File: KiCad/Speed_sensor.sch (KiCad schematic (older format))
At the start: 31 parts

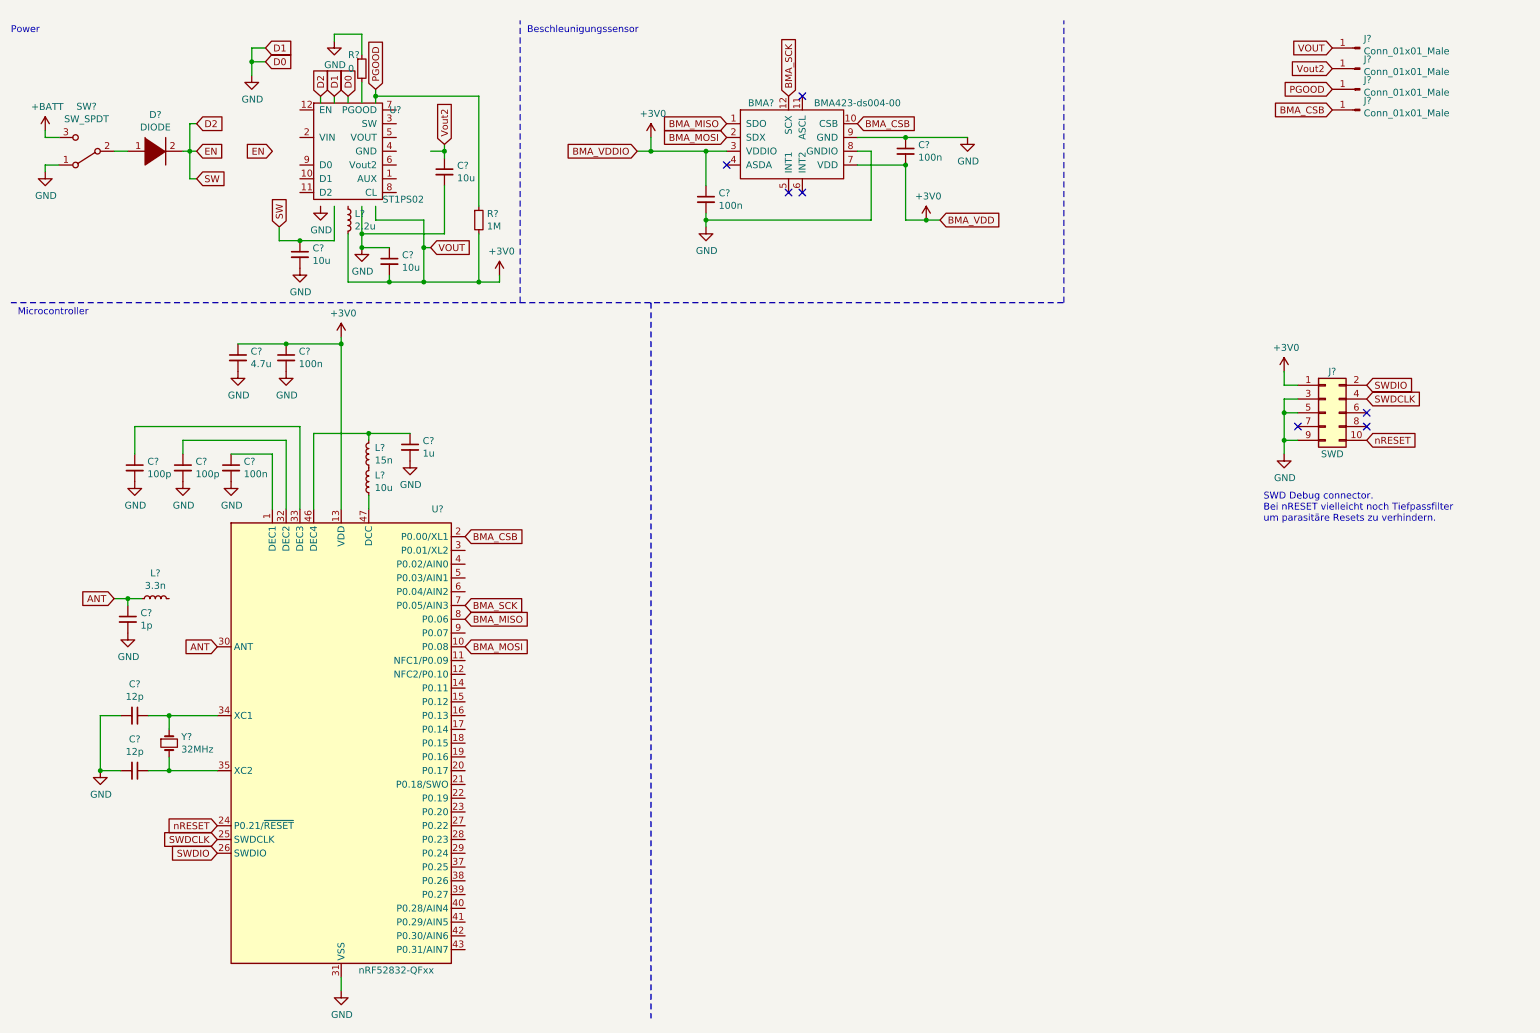
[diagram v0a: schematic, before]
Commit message: hierarchische Aufteilung der Schematic angefangen & power circuit um Battery management + usb connector erweitert
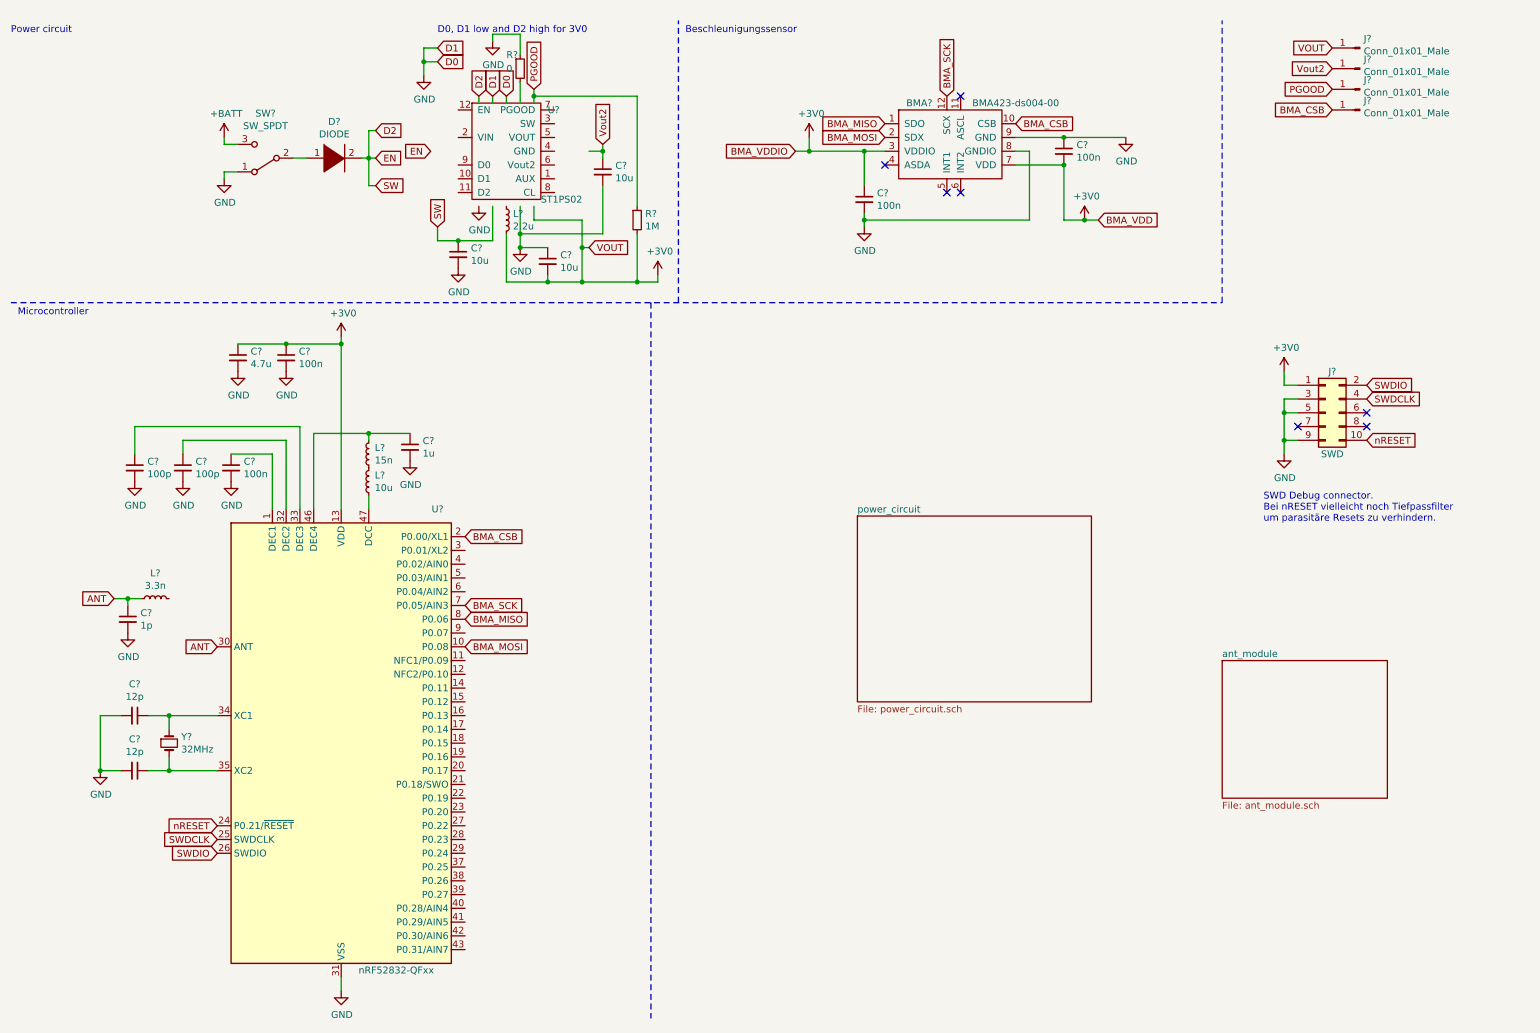
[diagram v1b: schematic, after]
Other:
- note added: "D0, D1 low and D2 high for 3V0"
- note added: "Power circuit"
- note removed: "Power"
- moved on the sheet: BMA?, C?, D?, L?, R?, SW?, U?

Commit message: Schematic ein bisschen sortiert
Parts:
- removed C? (x3): 10u, symbol Device:C_Small
- removed D?: DIODE, symbol pspice:DIODE
- removed J? (x4): Conn_01x01_Male, symbol Connector:Conn_01x01_Male
- removed L?: 2.2u, symbol Device:L_Small
- removed R?: 0, symbol Device:R_Small
- removed R?: 1M, symbol Device:R_Small
- removed SW?: SW_SPDT, symbol Switch:SW_SPDT
- removed U?: ST1PS02, symbol Nils_KiCADLibrary:ST1PS02
- added H?: VOUT, symbol Mechanical:MountingHole_Pad
- added H?: Vout2, symbol Mechanical:MountingHole_Pad
- added H?: PGOOD, symbol Mechanical:MountingHole_Pad
- added H?: BMA_CSB, symbol Mechanical:MountingHole_Pad
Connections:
- net labels removed: +BATT, D0, D1, D2, EN, SW
- wire segments 105 -> 54
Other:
- note removed: "D0, D1 low and D2 high for 3V0"
- note removed: "Power circuit"

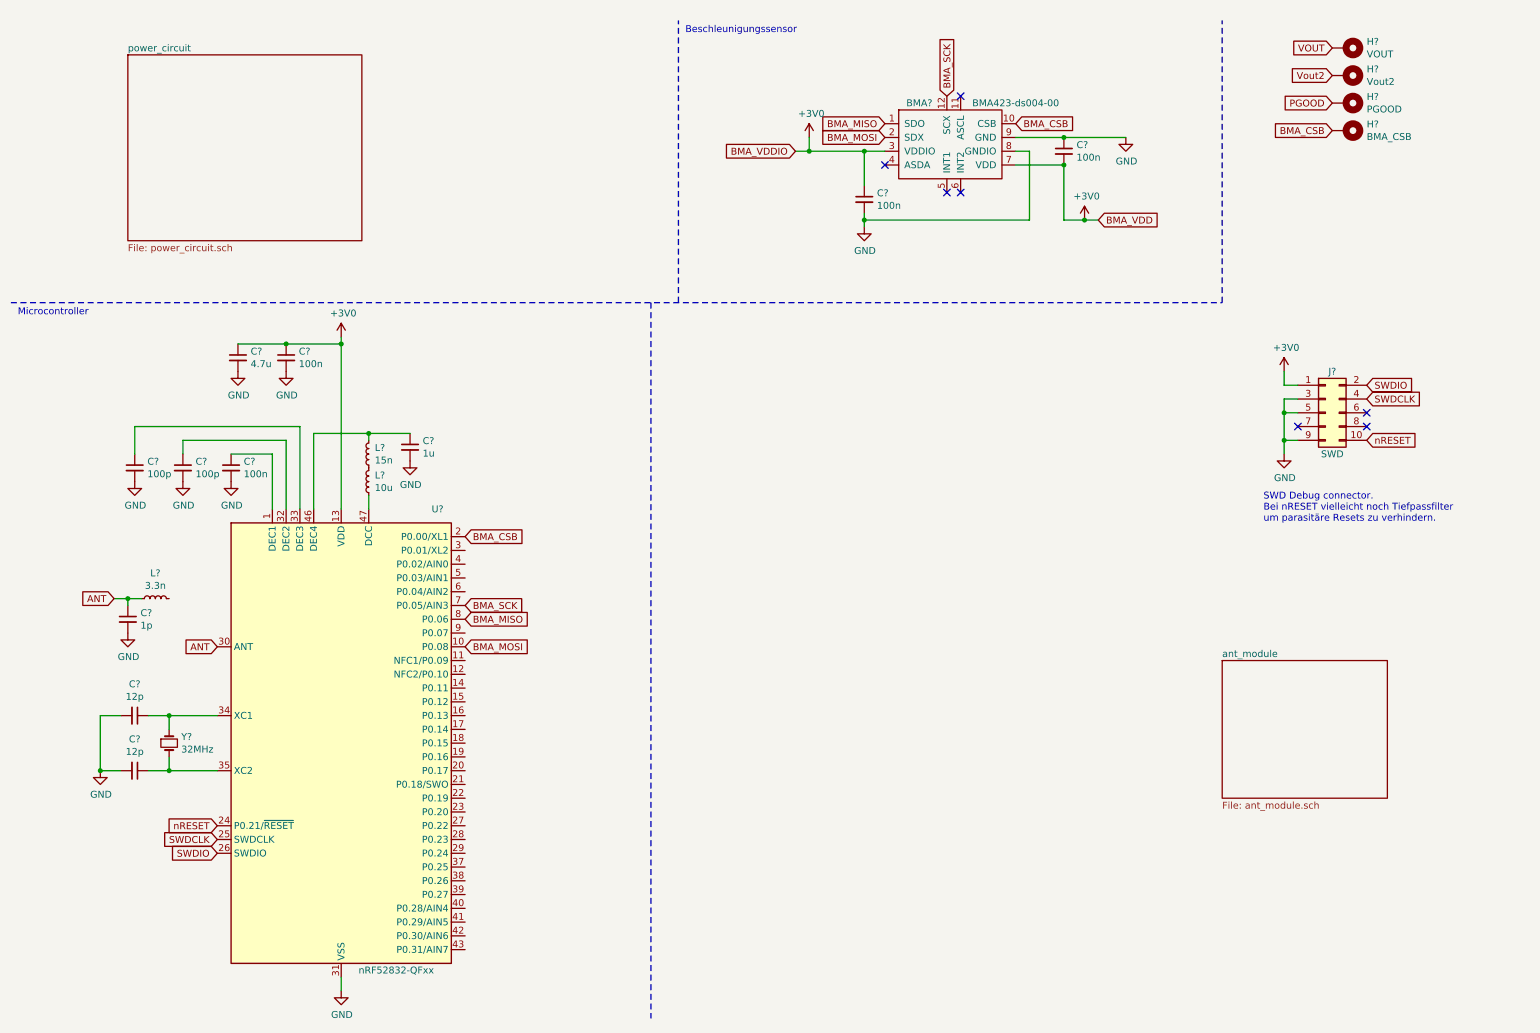
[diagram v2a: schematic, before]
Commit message: changed SPI labels to make it more general and not specific to the BMA Sensor
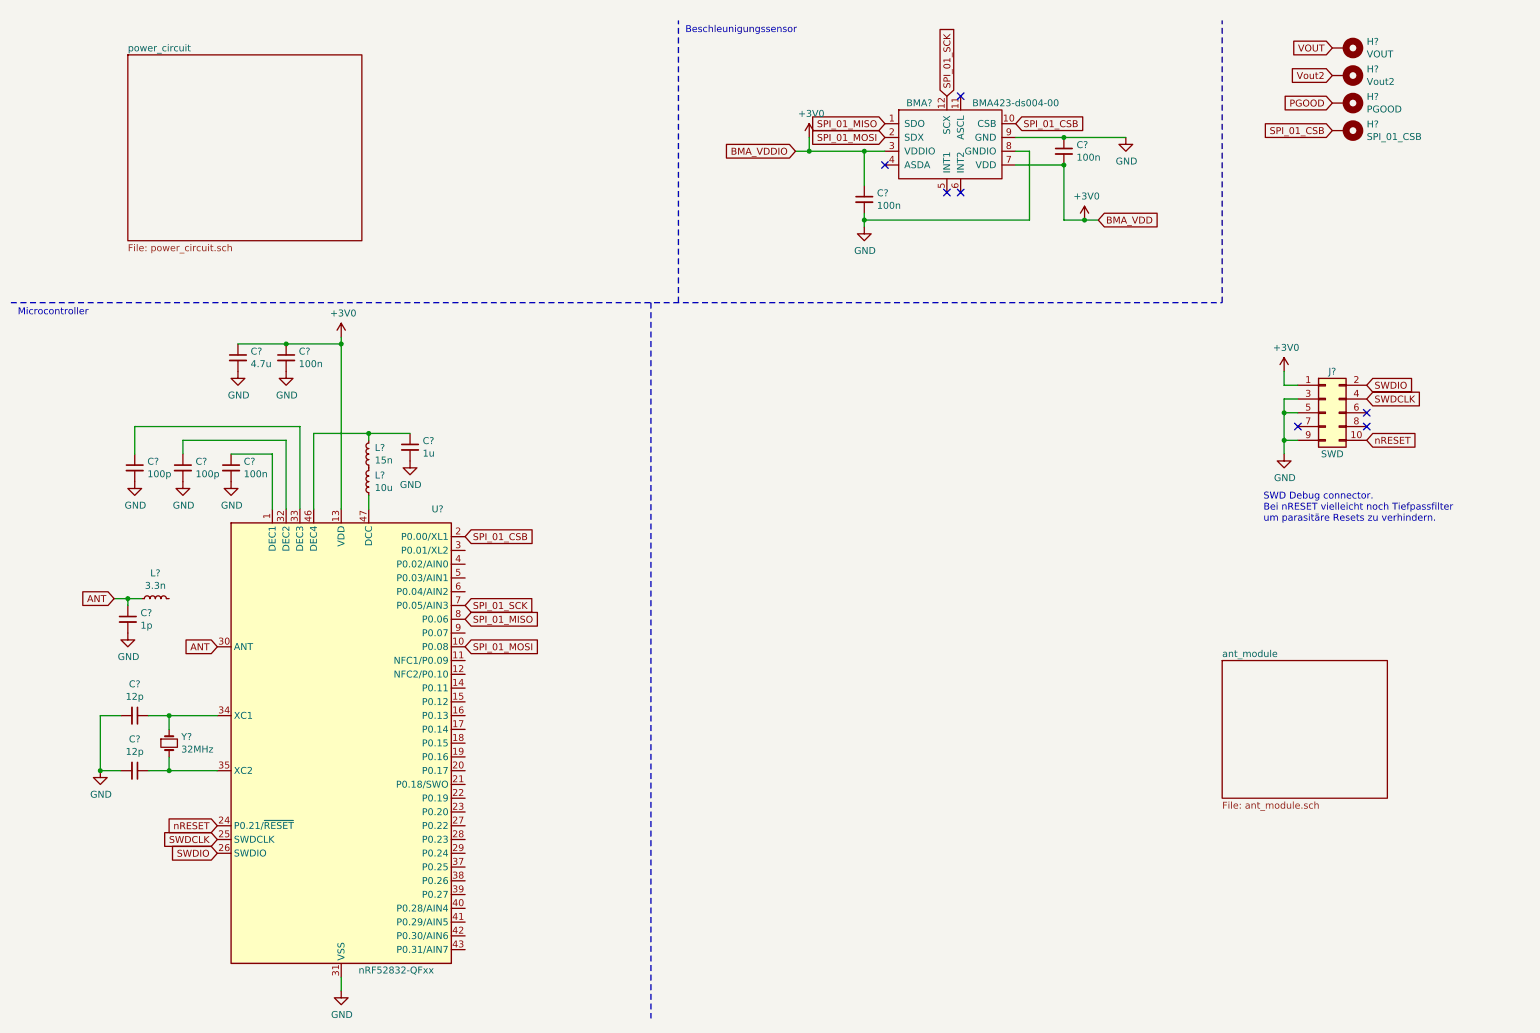
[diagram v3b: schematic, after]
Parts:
- H?: value BMA_CSB -> SPI_01_CSB
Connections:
- net BMA_CSB renamed SPI_01_CSB
- net BMA_MISO renamed SPI_01_MISO
- net BMA_MOSI renamed SPI_01_MOSI
- net BMA_SCK renamed SPI_01_SCK
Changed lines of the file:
@@
 BMA_VDDIO
 Connection ~ 6700 1450
-Text GLabel 6850 1350 0    50   Input ~ 0
-BMA_MOSI
-Text GLabel 7800 1250 2    50   Input ~ 0
-BMA_CSB
 NoConn ~ 7400 1050
 NoConn ~ 6850 1550
 Wire Wire Line
 	6700 1900 6700 1950
-Text GLabel 7300 1050 1    50   Input ~ 0
-BMA_SCK
-Text GLabel 6850 1250 0    50   Input ~ 0
-BMA_MISO
 Connection ~ 6700 1950
 Wire Wire Line
 	6700 1950 6700 2000
 Text GLabel 3800 4250 2    50   Input ~ 0
-BMA_CSB
-Text GLabel 3800 4750 2    50   Input ~ 0
-BMA_SCK
+SPI_01_CSB
 Text GLabel 3800 4850 2    50   Input ~ 0
-BMA_MISO
+SPI_01_MISO
 Text GLabel 3800 5050 2    50   Input ~ 0
-BMA_MOSI
+SPI_01_MOSI
 Wire Notes Line
 	9300 2550 9300 500
@@
 Wire Wire Line
 	6300 1450 6700 1450
-Text GLabel 10100 1300 0    50   Input ~ 0
-BMA_CSB
 Wire Wire Line
 	8150 1550 8150 1950
@@
 P 10200 1300
 F 0 "H?" V 10154 1450 50  0000 L CNN
-F 1 "BMA_CSB" V 10245 1450 50  0000 L CNN
+F 1 "SPI_01_CSB" V 10245 1450 50  0000 L CNN
 F 2 "" H 10200 1300 50  0001 C CNN
 F 3 "~" H 10200 1300 50  0001 C CNN
@@
 	0    1    1    0
 $EndComp
+Text GLabel 7800 1250 2    50   Input ~ 0
+SPI_01_CSB
+Text GLabel 10100 1300 0    50   Input ~ 0
+SPI_01_CSB
+Text GLabel 7300 1050 1    50   Input ~ 0
+SPI_01_SCK
+Text GLabel 3800 4750 2    50   Input ~ 0
+SPI_01_SCK
+Text GLabel 6850 1250 0    50   Input ~ 0
+SPI_01_MISO
+Text GLabel 6850 1350 0    50   Input ~ 0
+SPI_01_MOSI
 $EndSCHEMATC
